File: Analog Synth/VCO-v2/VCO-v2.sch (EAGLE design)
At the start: 121 parts, among them IC1 TL084P, IC2 TL084P, IC3 78L09, IC4 78L05, IC5 79L09\, IC6 79L05, IC7 TL084P, Q1 J310, Q2 J310, Q3 2N3904, Q4 2N3904, T1 2N3904, T2 2N3904, T3 2N3904, T4 2N3904, T7 2N3904, U1 CA3096

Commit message: VCO-v2 exported pdf for VCO-v2.0
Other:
- note added: "This triangle-to-sine converter is a modified version of Thomas Henry's design."
- note removed: "Triangle to Sine converter is a modified version of Thomas Henry's design."
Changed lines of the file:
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@@
 This part of the circuit processes the triangle wave nonlinearly to shape it into a fairly sineusoidal waveform.</description>
 <plain>
-<text x="-27.94" y="81.28" size="1.778" layer="97">Triangle to Sine converter is a modified
-version of Thomas Henry's design.</text>
+<text x="-30.48" y="81.28" size="1.778" layer="97">This triangle-to-sine converter is a
+modified version of Thomas Henry's design.</text>
 </plain>
 <instances>

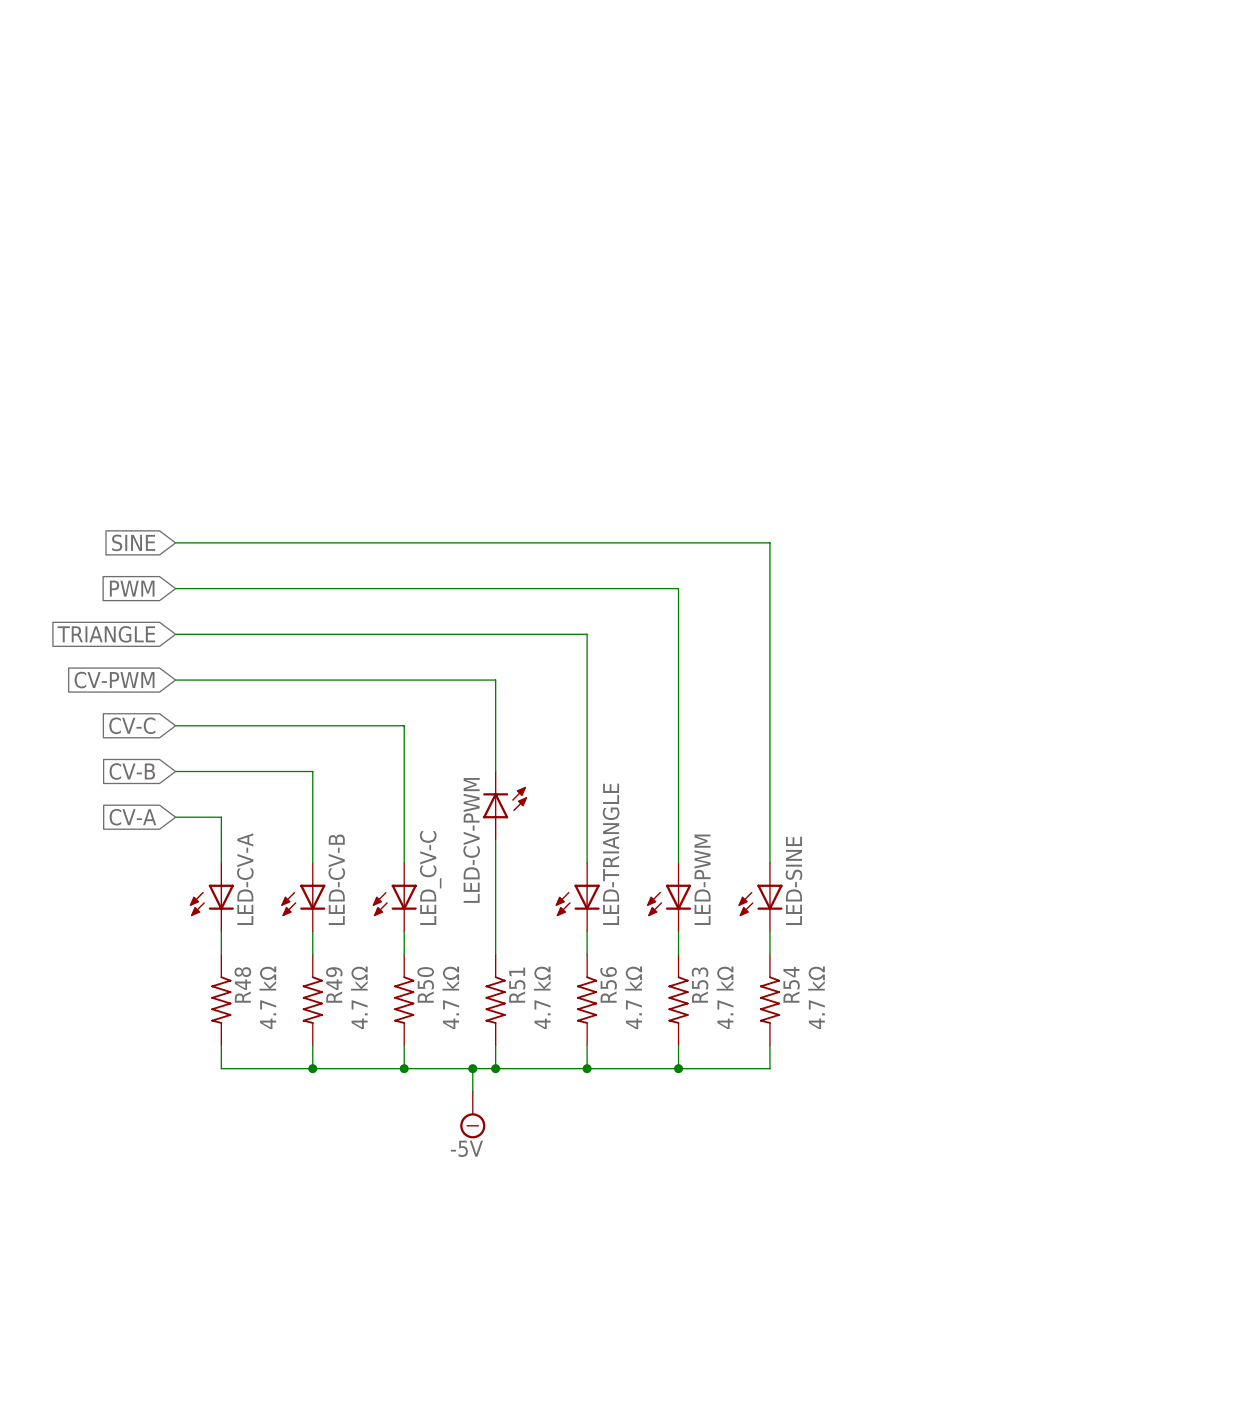
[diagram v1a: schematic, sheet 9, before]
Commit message: VCO-v2 - version 2.1 released! I changed a few things with the triangle-to-freq converter; I made the LEDs go into a bjt voltage source rather than the +5 V and -5 V regulated supplies, because connecting LEDs to those supply lines changed the frequency, and I'm not interested in that.
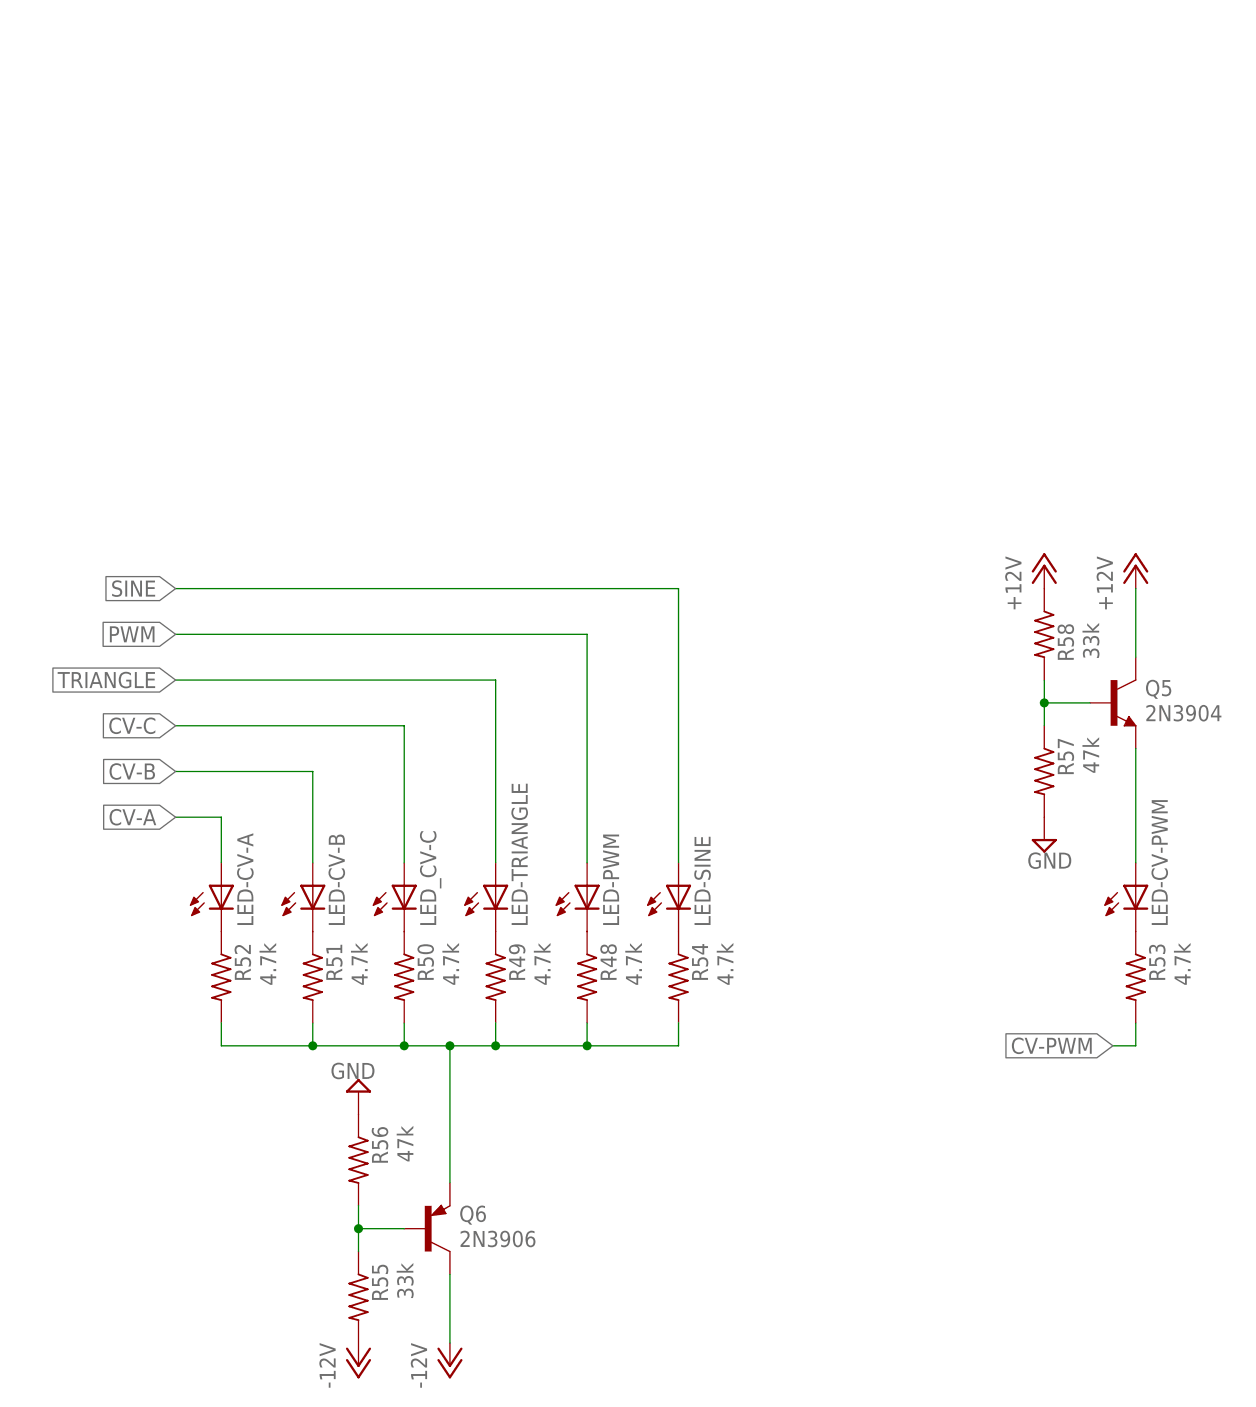
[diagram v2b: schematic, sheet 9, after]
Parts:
- added Q5: 2N3904, transistor-npn:2N3904
- added Q6: 2N3906, transistor-pnp:2N3906
- added R52: 4.7k, resistor:R-US_0204/7
- added R55, R58: 33k, resistor:R-US_0204/7
- added R57: 47k, resistor:R-US_0204/7
- ATTN-CV-PWM: value 100k lin -> 100k log
- R-SINE-AMPL, R-SINE-ROUND: value 100k lin -> 100k trim
- R-SINE-SYMM: value 10 kΩ -> 10k trim
- R39, R40: value 2.2 kΩ -> 2.2k
- R41: value 390 Ω -> 470
- R42: value 18 kΩ -> 100k
- R43, R44: value 10 kΩ -> 47k
- R45, R46: value 10 kΩ -> 10k
- R48, R49, R50, R51, R53, R54: value 4.7 kΩ -> 4.7k
- R56: value 4.7 kΩ -> 47k
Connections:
- new net N$11: LED-CV-PWM.C, R53.1
- new net N$5: Q6.B, R55.1, R56.2
- new net N$58: LED-CV-PWM.A, Q5.E
- new net N$7: Q6.E, R48.2, R49.2, R50.2, R51.2, R52.2, R54.2
- net +12V: now also Q5.C, R58.1
- net -12V: now also Q6.C, R55.2
- net -5V: no longer R48.2, R49.2, R50.2, R51.2, R53.2, R54.2, R56.2
- net CV-PWM: now also R53.2; no longer LED-CV-PWM.C
- net GND: now also R56.1, R57.2
- net N$44: now also Q5.B, R57.1, R58.2; no longer LED-CV-PWM.A, R51.1
- net N$53: now also R52.1; no longer R48.1
- net N$56: now also R51.1; no longer R49.1
- net N$59: now also R48.1; no longer R53.1
- net N$60: now also R49.1; no longer R56.1
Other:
- moved on the sheet: LED-CV-PWM, LED-PWM, LED-SINE, LED-TRIANGLE, R48, R49, R50, R51, R53, R54, R56

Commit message: VCO-v2
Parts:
- CV-A-MAN: value 10k lin -> 100k lin
- renumbered FREQ-MAN to CV-A-MAN
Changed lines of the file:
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@@
 <part name="R6" library="resistor" deviceset="R-US_" device="0204/7" value="47k"/>
 <part name="VLT/OCT-A" library="pot" deviceset="TRIM_US-" device="B64Y" value="10k trim"/>
-<part name="FREQ-MAN" library="pot" deviceset="TRIM_US-" device="B64Y" value="10k lin"/>
+<part name="CV-A-MAN" library="pot" deviceset="TRIM_US-" device="B64Y" value="100k lin"/>
 <part name="R11" library="resistor" deviceset="R-US_" device="0204/7" value="22k"/>
 <part name="R12" library="resistor" deviceset="R-US_" device="0204/7" value="1k"/>
@@
 <attribute name="VALUE" x="12.7" y="73.66" size="1.778" layer="96"/>
 </instance>
-<instance part="FREQ-MAN" gate="G$1" x="-45.72" y="96.52" smashed="yes" rot="R180">
+<instance part="CV-A-MAN" gate="G$1" x="-45.72" y="96.52" smashed="yes" rot="R180">
 <attribute name="NAME" x="-40.386" y="102.616" size="1.778" layer="95" rot="R270"/>
 <attribute name="VALUE" x="-43.18" y="101.6" size="1.778" layer="96" rot="R270"/>
@@
 <wire x1="-53.34" y1="71.12" x2="-53.34" y2="96.52" width="0.1524" layer="91"/>
 <wire x1="-53.34" y1="96.52" x2="-50.8" y2="96.52" width="0.1524" layer="91"/>
-<pinref part="FREQ-MAN" gate="G$1" pin="S"/>
+<pinref part="CV-A-MAN" gate="G$1" pin="S"/>
 </segment>
 </net>
@@
 <segment>
 <pinref part="SUPPLY1" gate="+5V" pin="+5V"/>
-<pinref part="FREQ-MAN" gate="G$1" pin="A"/>
+<pinref part="CV-A-MAN" gate="G$1" pin="A"/>
 </segment>
 </net>
@@
 <segment>
 <pinref part="SUPPLY2" gate="-5V" pin="-5V"/>
-<pinref part="FREQ-MAN" gate="G$1" pin="E"/>
+<pinref part="CV-A-MAN" gate="G$1" pin="E"/>
 </segment>
 <segment>
@@
 </instance>
 <instance part="Q3" gate="G1" x="12.7" y="35.56" smashed="yes">
-<attribute name="NAME" x="15.748" y="40.386" size="1.778" layer="95"/>
-<attribute name="VALUE" x="16.002" y="37.592" size="1.778" layer="96"/>
+<attribute name="NAME" x="16.256" y="40.132" size="1.778" layer="95"/>
+<attribute name="VALUE" x="16.002" y="37.084" size="1.778" layer="96"/>
 </instance>
 <instance part="Q4" gate="G1" x="38.1" y="35.56" smashed="yes" rot="MR0">
-<attribute name="NAME" x="34.544" y="40.132" size="1.778" layer="95" rot="MR0"/>
-<attribute name="VALUE" x="34.544" y="37.592" size="1.778" layer="96" rot="MR0"/>
+<attribute name="NAME" x="42.672" y="39.37" size="1.778" layer="95" rot="MR0"/>
+<attribute name="VALUE" x="48.768" y="36.322" size="1.778" layer="96" rot="MR0"/>
 </instance>
 <instance part="R40" gate="G$1" x="43.18" y="27.94" smashed="yes" rot="R270">
@@
 </instance>
 <instance part="R41" gate="G$1" x="25.4" y="27.94" smashed="yes">
-<attribute name="NAME" x="21.59" y="29.4386" size="1.778" layer="95"/>
-<attribute name="VALUE" x="21.59" y="32.258" size="1.778" layer="96"/>
+<attribute name="NAME" x="23.114" y="29.6926" size="1.778" layer="95"/>
+<attribute name="VALUE" x="23.114" y="32.258" size="1.778" layer="96"/>
 </instance>
 <instance part="R-SINE-SYMM" gate="G$1" x="25.4" y="17.78" smashed="yes" rot="R270">

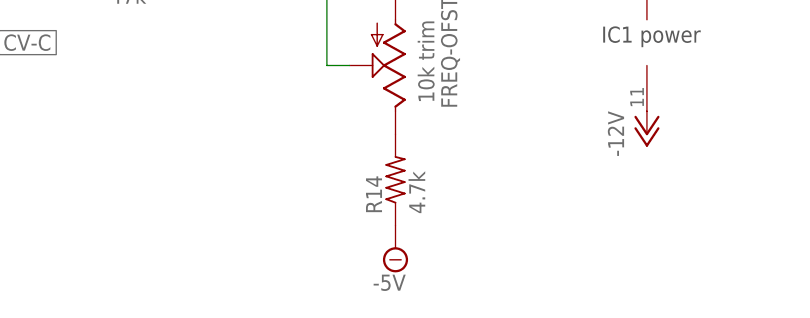
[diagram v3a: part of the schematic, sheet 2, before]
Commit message: fixed error in VCO-v2 schematic - CV sum had a tuner going to -5 V instead of -9 V
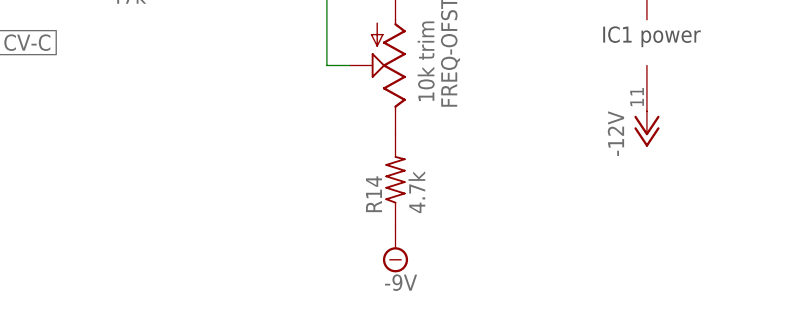
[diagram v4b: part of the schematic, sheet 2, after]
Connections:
- net -5V: no longer R14.1
- net -9V: now also R14.1
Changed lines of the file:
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@@
 <part name="FREQ-OFST" library="pot" deviceset="TRIM_US-" device="B64Y" value="10k trim"/>
 <part name="R14" library="resistor" deviceset="R-US_" device="0204/7" value="4.7k"/>
-<part name="SUPPLY7" library="supply2" deviceset="-5V" device=""/>
 <part name="ATTN_CV_B" library="pot" deviceset="TRIM_US-" device="B64Y" value="100k log"/>
 <part name="ATTN_CV_C" library="pot" deviceset="TRIM_US-" device="B64Y" value="100k log"/>
@@
 <part name="R58" library="resistor" deviceset="R-US_" device="0204/7" value="33k"/>
 <part name="P+7" library="supply1" deviceset="+12V" device=""/>
+<part name="SUPPLY7" library="supply2" deviceset="-9V" device=""/>
 </parts>
 <sheets>
@@
 </instance>
 <instance part="R14" gate="G$1" x="30.48" y="2.54" rot="R90"/>
-<instance part="SUPPLY7" gate="-5V" x="30.48" y="-5.08"/>
 <instance part="ATTN_CV_B" gate="G$1" x="-60.96" y="43.18" smashed="yes">
 <attribute name="NAME" x="-66.04" y="35.56" size="1.778" layer="95" rot="R90"/>
@@
 <instance part="P+4" gate="1" x="58.42" y="27.94"/>
 <instance part="P-2" gate="1" x="58.42" y="7.62"/>
+<instance part="SUPPLY7" gate="G$1" x="30.48" y="-5.08"/>
 </instances>
 <busses>
@@
 <wire x1="35.56" y1="40.64" x2="35.56" y2="38.1" width="0.1524" layer="91"/>
 </segment>
-<segment>
-<pinref part="R14" gate="G$1" pin="1"/>
-<pinref part="SUPPLY7" gate="-5V" pin="-5V"/>
-</segment>
 </net>
 <net name="NPN_CV" class="0">
@@
 </segment>
 </net>
+<net name="-9V" class="0">
+<segment>
+<pinref part="R14" gate="G$1" pin="1"/>
+<pinref part="SUPPLY7" gate="G$1" pin="-9V"/>
+</segment>
+</net>

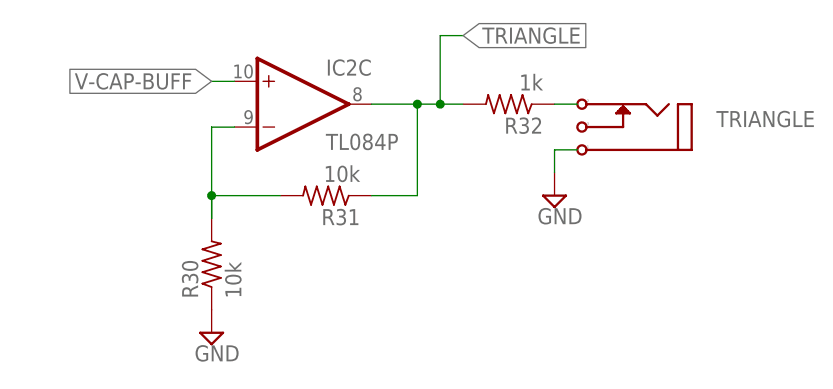
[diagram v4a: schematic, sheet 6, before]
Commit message: VCO-v2 - increased size of resistors around the triangle-wave x2 gain stage
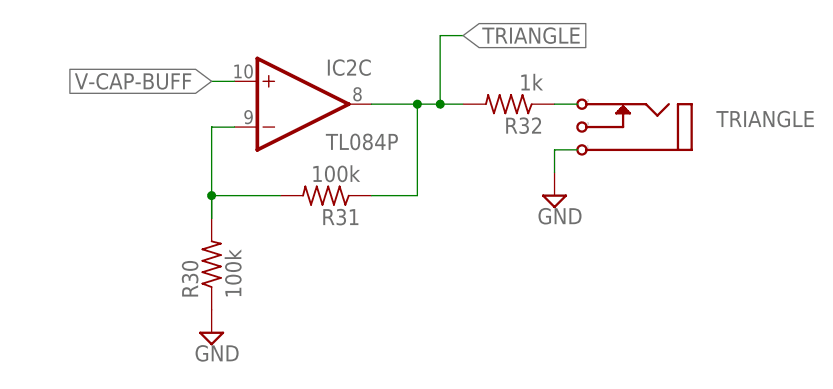
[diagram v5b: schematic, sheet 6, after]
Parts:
- R30, R31: value 10k -> 100k
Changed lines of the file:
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@@
 <part name="P-6" library="supply1" deviceset="-12V" device=""/>
 <part name="SUPPLY34" library="supply2" deviceset="GND" device=""/>
-<part name="R30" library="resistor" deviceset="R-US_" device="0204/7" value="10k"/>
-<part name="R31" library="resistor" deviceset="R-US_" device="0204/7" value="10k"/>
+<part name="R30" library="resistor" deviceset="R-US_" device="0204/7" value="100k"/>
+<part name="R31" library="resistor" deviceset="R-US_" device="0204/7" value="100k"/>
 <part name="TRIANGLE" library="!synth_sch" deviceset="MONO_JACK" device="" value="I/O"/>
 <part name="SUPPLY35" library="supply2" deviceset="GND" device=""/>
